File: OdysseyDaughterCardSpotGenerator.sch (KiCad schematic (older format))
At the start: 20 parts, among them Q1 2N3904, Q2 2N3904, Q3 BC547C, Q4 2N3904, X1 OdysseyDaughterCard

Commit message: Layout components on PCB
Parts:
- C1, C2, C4, C5: footprint (none) -> Capacitor_THT:C_Rect_L4.0mm_W2.5mm_P2.50mm
- C3: footprint (none) -> Capacitor_THT:C_Rect_L4.6mm_W5.5mm_P2.50mm_MKS02_FKP02
- R1, R2, R3, R4, R5, R6, R7, R8: footprint (none) -> Resistor_THT:R_Axial_DIN0207_L6.3mm_D2.5mm_P7.62mm_Horizontal
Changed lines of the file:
@@
 F 0 "R1" V 3293 3700 50  0000 C CNN
 F 1 "10k" V 3384 3700 50  0000 C CNN
-F 2 "" V 3430 3700 50  0001 C CNN
+F 2 "Resistor_THT:R_Axial_DIN0207_L6.3mm_D2.5mm_P7.62mm_Horizontal" V 3430 3700 50  0001 C CNN
 F 3 "~" H 3500 3700 50  0001 C CNN
 	1    3500 3700
@@
 F 0 "R2" H 4280 3854 50  0000 R CNN
 F 1 "100K" H 4280 3945 50  0000 R CNN
-F 2 "" V 4280 3900 50  0001 C CNN
+F 2 "Resistor_THT:R_Axial_DIN0207_L6.3mm_D2.5mm_P7.62mm_Horizontal" V 4280 3900 50  0001 C CNN
 F 3 "~" H 4350 3900 50  0001 C CNN
 	1    4350 3900
@@
 F 0 "R6" H 4280 4354 50  0000 R CNN
 F 1 "270K" H 4280 4445 50  0000 R CNN
-F 2 "" V 4280 4400 50  0001 C CNN
+F 2 "Resistor_THT:R_Axial_DIN0207_L6.3mm_D2.5mm_P7.62mm_Horizontal" V 4280 4400 50  0001 C CNN
 F 3 "~" H 4350 4400 50  0001 C CNN
 	1    4350 4400
@@
 F 0 "C1" V 3698 3700 50  0000 C CNN
 F 1 "1500p" V 3789 3700 50  0000 C CNN
-F 2 "" H 3988 3550 50  0001 C CNN
+F 2 "Capacitor_THT:C_Rect_L4.0mm_W2.5mm_P2.50mm" H 3988 3550 50  0001 C CNN
 F 3 "~" H 3950 3700 50  0001 C CNN
 	1    3950 3700
@@
 F 0 "R3" H 5430 3904 50  0000 R CNN
 F 1 "10k" H 5430 3995 50  0000 R CNN
-F 2 "" V 5430 3950 50  0001 C CNN
+F 2 "Resistor_THT:R_Axial_DIN0207_L6.3mm_D2.5mm_P7.62mm_Horizontal" V 5430 3950 50  0001 C CNN
 F 3 "~" H 5500 3950 50  0001 C CNN
 	1    5500 3950
@@
 F 0 "R7" H 5430 4404 50  0000 R CNN
 F 1 "10k" H 5430 4495 50  0000 R CNN
-F 2 "" V 5430 4450 50  0001 C CNN
+F 2 "Resistor_THT:R_Axial_DIN0207_L6.3mm_D2.5mm_P7.62mm_Horizontal" V 5430 4450 50  0001 C CNN
 F 3 "~" H 5500 4450 50  0001 C CNN
 	1    5500 4450
@@
 F 0 "C4" V 6002 4850 50  0000 C CNN
 F 1 "0.1u" V 5911 4850 50  0000 C CNN
-F 2 "" H 5788 4700 50  0001 C CNN
+F 2 "Capacitor_THT:C_Rect_L4.0mm_W2.5mm_P2.50mm" H 5788 4700 50  0001 C CNN
 F 3 "~" H 5750 4850 50  0001 C CNN
 	1    5750 4850
@@
 F 0 "C5" H 6265 5146 50  0000 L CNN
 F 1 "0.01u" H 6265 5055 50  0000 L CNN
-F 2 "" H 6188 4950 50  0001 C CNN
+F 2 "Capacitor_THT:C_Rect_L4.0mm_W2.5mm_P2.50mm" H 6188 4950 50  0001 C CNN
 F 3 "~" H 6150 5100 50  0001 C CNN
 	1    6150 5100
@@
 F 0 "R8" V 7357 5400 50  0000 C CNN
 F 1 "10k" V 7266 5400 50  0000 C CNN
-F 2 "" V 7080 5400 50  0001 C CNN
+F 2 "Resistor_THT:R_Axial_DIN0207_L6.3mm_D2.5mm_P7.62mm_Horizontal" V 7080 5400 50  0001 C CNN
 F 3 "~" H 7150 5400 50  0001 C CNN
 	1    7150 5400
@@
 F 0 "R4" V 6707 4250 50  0000 C CNN
 F 1 "2.2k" V 6616 4250 50  0000 C CNN
-F 2 "" V 6430 4250 50  0001 C CNN
+F 2 "Resistor_THT:R_Axial_DIN0207_L6.3mm_D2.5mm_P7.62mm_Horizontal" V 6430 4250 50  0001 C CNN
 F 3 "~" H 6500 4250 50  0001 C CNN
 	1    6500 4250
@@
 F 0 "R5" V 7407 4250 50  0000 C CNN
 F 1 "10k" V 7316 4250 50  0000 C CNN
-F 2 "" V 7130 4250 50  0001 C CNN
+F 2 "Resistor_THT:R_Axial_DIN0207_L6.3mm_D2.5mm_P7.62mm_Horizontal" V 7130 4250 50  0001 C CNN
 F 3 "~" H 7200 4250 50  0001 C CNN
 	1    7200 4250
@@
 F 0 "C2" V 5598 3700 50  0000 C CNN
 F 1 "120p" V 5689 3700 50  0000 C CNN
-F 2 "" H 5888 3550 50  0001 C CNN
+F 2 "Capacitor_THT:C_Rect_L4.0mm_W2.5mm_P2.50mm" H 5888 3550 50  0001 C CNN
 F 3 "~" H 5850 3700 50  0001 C CNN
 	1    5850 3700
@@
 F 0 "C3" H 4235 5054 50  0000 R CNN
 F 1 "0.15u" H 4235 5145 50  0000 R CNN
-F 2 "" H 4388 4950 50  0001 C CNN
+F 2 "Capacitor_THT:C_Rect_L4.6mm_W5.5mm_P2.50mm_MKS02_FKP02" H 4388 4950 50  0001 C CNN
 F 3 "~" H 4350 5100 50  0001 C CNN
 	1    4350 5100

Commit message: 1.0 add port for emulator team
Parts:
- added J1: Conn_01x03, Connector_PinHeader_2.54mm:PinHeader_1x03_P2.54mm_Vertical, symbol Connector_Generic:Conn_01x03
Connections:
- net Card2: now also J1.1 (Pin_1)
- net Card9: now also J1.2 (Pin_2)
- net GND: now also J1.3 (Pin_3)
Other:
- note added: "For sampling of player spot\nposition by emulator team"
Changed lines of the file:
@@
 encoding utf-8
 Sheet 1 1
-Title "Odyssey Daughter Card Template"
-Date "2018-05-29"
-Rev "0.1"
+Title "Odyssey Daughter Card Spot Generator"
+Date "2018-09-29"
+Rev "1.0"
 Comp "University of Pittsburgh - Odyssey Restoration Project"
 Comment1 "Levi Burner"
@@
 Text Label 5950 5550 3    60   ~ 0
 Card4
+$Comp
+L Connector_Generic:Conn_01x03 J1
+U 1 1 5BB036BF
+P 8350 2250
+F 0 "J1" H 8430 2292 50  0000 L CNN
+F 1 "Conn_01x03" H 8430 2201 50  0000 L CNN
+F 2 "Connector_PinHeader_2.54mm:PinHeader_1x03_P2.54mm_Vertical" H 8350 2250 50  0001 C CNN
+F 3 "~" H 8350 2250 50  0001 C CNN
+	1    8350 2250
+	1    0    0    -1
+$EndComp
+Wire Wire Line
+	8150 2350 7850 2350
+Wire Wire Line
+	7850 2350 7850 2500
+$Comp
+L power:GND #PWR06
+U 1 1 5BB0543B
+P 7850 2500
+F 0 "#PWR06" H 7850 2250 50  0001 C CNN
+F 1 "GND" H 7855 2327 50  0000 C CNN
+F 2 "" H 7850 2500 50  0001 C CNN
+F 3 "" H 7850 2500 50  0001 C CNN
+	1    7850 2500
+	1    0    0    -1
+$EndComp
+Wire Wire Line
+	8150 2250 7850 2250
+Wire Wire Line
+	8150 2150 7850 2150
+Text Label 7850 2150 2    60   ~ 0
+Card2
+Text Label 7850 2250 2    60   ~ 0
+Card9
+Text Notes 7650 1950 0    60   ~ 0
+For sampling of player spot\nposition by emulator team
 $EndSCHEMATC

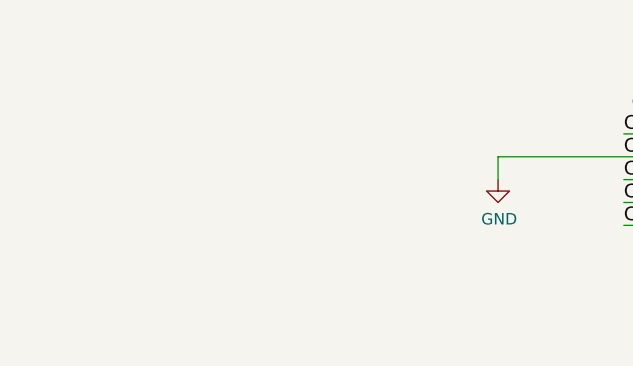
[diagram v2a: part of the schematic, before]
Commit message: R1.1 add header for extra player gen
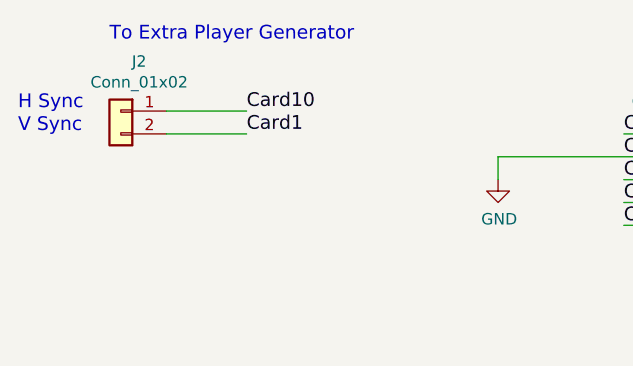
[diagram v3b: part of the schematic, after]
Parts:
- added J2: Conn_01x02, Connector_PinHeader_2.54mm:PinHeader_1x02_P2.54mm_Vertical, symbol Connector_Generic:Conn_01x02
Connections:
- net Card1: now also J2.2 (Pin_2)
- net Card10: now also J2.1 (Pin_1)
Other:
- note added: "H Sync"
- note added: "To Extra Player Generator"
- note added: "V Sync"
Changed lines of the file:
@@
 Sheet 1 1
 Title "Odyssey Daughter Card Spot Generator"
-Date "2018-09-29"
-Rev "1.0"
+Date "2018-11-23"
+Rev "1.1"
 Comp "University of Pittsburgh - Odyssey Restoration Project"
 Comment1 "Levi Burner"
@@
 Text Notes 7650 1950 0    60   ~ 0
 For sampling of player spot\nposition by emulator team
+$Comp
+L Connector_Generic:Conn_01x02 J2
+U 1 1 5BF93A6E
+P 3050 2150
+F 0 "J2" H 2970 2367 50  0000 C CNN
+F 1 "Conn_01x02" H 2970 2276 50  0000 C CNN
+F 2 "Connector_PinHeader_2.54mm:PinHeader_1x02_P2.54mm_Vertical" H 3050 2150 50  0001 C CNN
+F 3 "~" H 3050 2150 50  0001 C CNN
+	1    3050 2150
+	-1   0    0    -1
+$EndComp
+Wire Wire Line
+	3250 2150 3600 2150
+Wire Wire Line
+	3250 2250 3600 2250
+Text Label 3600 2150 0    60   ~ 0
+Card10
+Text Label 3600 2250 0    60   ~ 0
+Card1
+Text Notes 3000 1850 0    60   ~ 0
+To Extra Player Generator
+Text Notes 2600 2150 0    60   ~ 0
+H Sync
+Text Notes 2600 2250 0    60   ~ 0
+V Sync
 $EndSCHEMATC

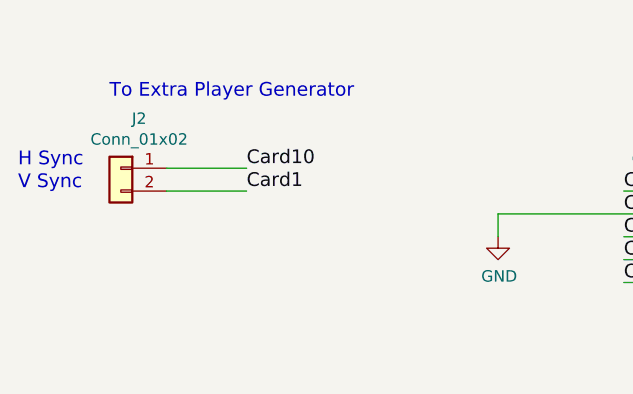
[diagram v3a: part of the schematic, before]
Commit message: Add gnd and vdd to extra player interface port still R1.2
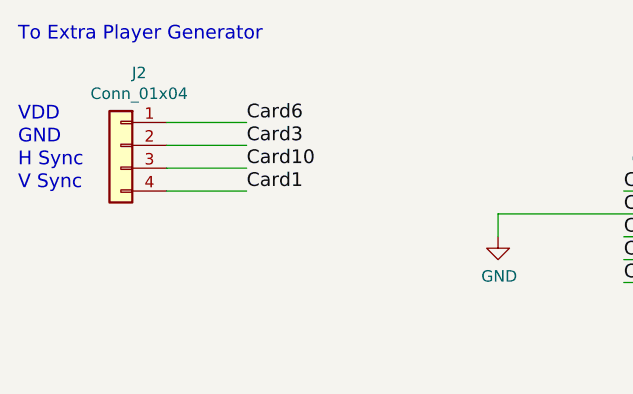
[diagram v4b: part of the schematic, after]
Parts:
- removed J2: Conn_01x02, Connector_PinHeader_2.54mm:PinHeader_1x02_P2.54mm_Vertical, symbol Connector_Generic:Conn_01x02
- added J2: Conn_01x04, Connector_PinHeader_2.54mm:PinHeader_1x04_P2.54mm_Vertical, symbol Connector_Generic:Conn_01x04
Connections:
- net Card1: now also J2.4 (Pin_4)
- net Card10: now also J2.3 (Pin_3)
- net Card6: now also J2.1 (Pin_1)
- net GND: now also J2.2 (Pin_2)
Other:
- note added: "GND"
- note added: "VDD"
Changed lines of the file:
@@
 Sheet 1 1
 Title "Odyssey Daughter Card Spot Generator"
-Date "2018-11-23"
-Rev "1.1"
+Date "2019-02-16"
+Rev "1.2"
 Comp "University of Pittsburgh - Odyssey Restoration Project"
 Comment1 "Levi Burner"
@@
 Text Notes 7650 1950 0    60   ~ 0
 For sampling of player spot\nposition by emulator team
-$Comp
-L Connector_Generic:Conn_01x02 J2
-U 1 1 5BF93A6E
-P 3050 2150
-F 0 "J2" H 2970 2367 50  0000 C CNN
-F 1 "Conn_01x02" H 2970 2276 50  0000 C CNN
-F 2 "Connector_PinHeader_2.54mm:PinHeader_1x02_P2.54mm_Vertical" H 3050 2150 50  0001 C CNN
-F 3 "~" H 3050 2150 50  0001 C CNN
-	1    3050 2150
-	-1   0    0    -1
-$EndComp
 Wire Wire Line
 	3250 2150 3600 2150
@@
 Text Label 3600 2250 0    60   ~ 0
 Card1
-Text Notes 3000 1850 0    60   ~ 0
+Text Notes 2600 1600 0    60   ~ 0
 To Extra Player Generator
 Text Notes 2600 2150 0    60   ~ 0
@@
 Text Notes 2600 2250 0    60   ~ 0
 V Sync
+$Comp
+L Connector_Generic:Conn_01x04 J2
+U 1 1 5C69F9A0
+P 3050 2050
+F 0 "J2" H 2970 2367 50  0000 C CNN
+F 1 "Conn_01x04" H 2970 2276 50  0000 C CNN
+F 2 "Connector_PinHeader_2.54mm:PinHeader_1x04_P2.54mm_Vertical" H 3050 2050 50  0001 C CNN
+F 3 "~" H 3050 2050 50  0001 C CNN
+	1    3050 2050
+	-1   0    0    -1
+$EndComp
+Wire Wire Line
+	3250 1950 3600 1950
+Wire Wire Line
+	3250 2050 3600 2050
+Text Label 3600 1950 0    60   ~ 0
+Card6
+Text Label 3600 2050 0    60   ~ 0
+Card3
+Text Notes 2600 2050 0    60   ~ 0
+GND
+Text Notes 2600 1950 0    60   ~ 0
+VDD
 $EndSCHEMATC
